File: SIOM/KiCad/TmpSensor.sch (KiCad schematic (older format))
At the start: 3 parts, among them U201 DS2482-800

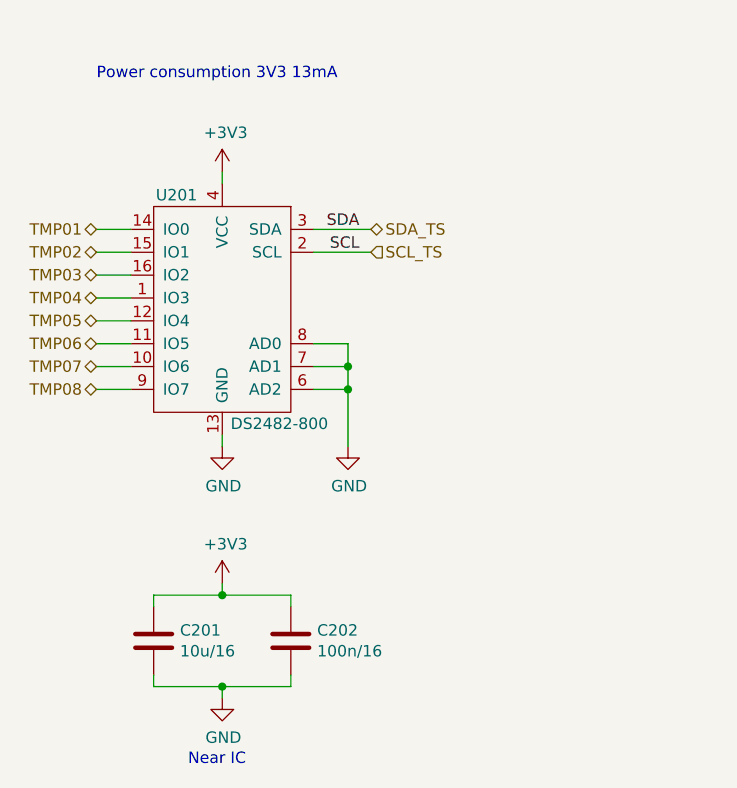
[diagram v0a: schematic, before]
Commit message: KiCad files SIOM_def
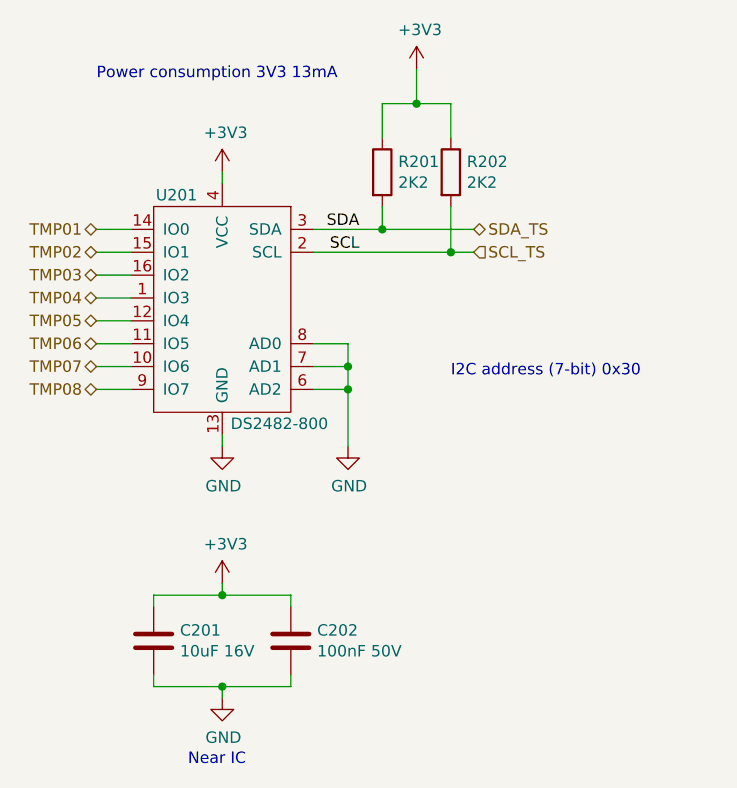
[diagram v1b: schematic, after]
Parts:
- added R201, R202: 2K2, Resistor_SMD:R_0603_1608Metric, symbol SIOMv01-rescue:R-Device
- C201: value 10u/16 -> 10uF 16V
- C202: value 100n/16 -> 100nF 50V
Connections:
- net +3V3: now also R201.1, R202.1
- net SCL_TS: now also R202.2
- net SDA_TS: now also R201.2
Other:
- note added: "I2C address (7-bit) 0x30"
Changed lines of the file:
@@
 EESchema Schematic File Version 4
-LIBS:SIOMv01-cache
 EELAYER 30 0
 EELAYER END
 $Descr A4 11693 8268
 encoding utf-8
-Sheet 2 9
+Sheet 2 10
 Title ""
 Date ""
@@
 $EndComp
 $Comp
-L SIOMv01-rescue:GND-power #PWR0203
+L SIOMv01-rescue:GND-power #PWR0205
 U 1 1 5FB29A98
 P 6600 4200
-F 0 "#PWR0203" H 6600 3950 50  0001 C CNN
+F 0 "#PWR0205" H 6600 3950 50  0001 C CNN
 F 1 "GND" H 6605 4027 50  0000 C CNN
 F 2 "" H 6600 4200 50  0001 C CNN
@@
 AR Path="/5F8C23BC/5FB2DA93" Ref="C201"  Part="1"
 F 0 "C201" H 5865 5096 50  0000 L CNN
-F 1 "10u/16" H 5865 5005 50  0000 L CNN
+F 1 "10uF 16V" H 5865 5005 50  0000 L CNN
 F 2 "Capacitor_SMD:C_0805_2012Metric" H 5788 4900 50  0001 C CNN
 F 3 "~" H 5750 5050 50  0001 C CNN
@@
 AR Path="/5FB2DA99" Ref="#PWR?"  Part="1"
 AR Path="/5F8BACBE/5FB2DA99" Ref="#PWR?"  Part="1"
-AR Path="/5F8C23BC/5FB2DA99" Ref="#PWR0205"  Part="1"
-F 0 "#PWR0205" H 6050 5050 50  0001 C CNN
+AR Path="/5F8C23BC/5FB2DA99" Ref="#PWR0204"  Part="1"
+F 0 "#PWR0204" H 6050 5050 50  0001 C CNN
 F 1 "GND" H 6055 5127 50  0000 C CNN
 F 2 "" H 6050 5300 50  0001 C CNN
@@
 P 6050 4800
 AR Path="/5F8BACBE/5FB2DAA1" Ref="#PWR?"  Part="1"
-AR Path="/5F8C23BC/5FB2DAA1" Ref="#PWR0204"  Part="1"
-F 0 "#PWR0204" H 6050 4650 50  0001 C CNN
+AR Path="/5F8C23BC/5FB2DAA1" Ref="#PWR0203"  Part="1"
+F 0 "#PWR0203" H 6050 4650 50  0001 C CNN
 F 1 "+3V3" H 6065 4973 50  0000 C CNN
 F 2 "" H 6050 4800 50  0001 C CNN
@@
 AR Path="/5F8C23BC/5FB6A68F" Ref="C202"  Part="1"
 F 0 "C202" H 6465 5096 50  0000 L CNN
-F 1 "100n/16" H 6465 5005 50  0000 L CNN
+F 1 "100nF 50V" H 6465 5005 50  0000 L CNN
 F 2 "Capacitor_SMD:C_0603_1608Metric" H 6388 4900 50  0001 C CNN
 F 3 "~" H 6350 5050 50  0001 C CNN
@@
 Text Notes 5900 5600 0    50   ~ 0
 Near IC
-Text HLabel 6700 3350 2    50   Input ~ 0
+Text HLabel 7150 3350 2    50   Input ~ 0
 SCL_TS
 Text Label 6650 3250 2    50   ~ 0
@@
 SCL
 Wire Wire Line
-	6450 3350 6700 3350
-Wire Wire Line
-	6450 3250 6700 3250
-Text HLabel 6700 3250 2    50   BiDi ~ 0
+	6450 3350 7050 3350
+Wire Wire Line
+	6450 3250 6750 3250
+Text HLabel 7150 3250 2    50   BiDi ~ 0
 SDA_TS
+$Comp
+L SIOMv01-rescue:R-Device R201
+U 1 1 6077B12F
+P 6750 3000
+F 0 "R201" H 6820 3046 50  0000 L CNN
+F 1 "2K2" H 6820 2955 50  0000 L CNN
+F 2 "Resistor_SMD:R_0603_1608Metric" V 6680 3000 50  0001 C CNN
+F 3 "~" H 6750 3000 50  0001 C CNN
+	1    6750 3000
+	1    0    0    -1
+$EndComp
+$Comp
+L SIOMv01-rescue:R-Device R202
+U 1 1 6077BA72
+P 7050 3000
+F 0 "R202" H 7120 3046 50  0000 L CNN
+F 1 "2K2" H 7120 2955 50  0000 L CNN
+F 2 "Resistor_SMD:R_0603_1608Metric" V 6980 3000 50  0001 C CNN
+F 3 "~" H 7050 3000 50  0001 C CNN
+	1    7050 3000
+	1    0    0    -1
+$EndComp
+Wire Wire Line
+	6750 3150 6750 3250
+Connection ~ 6750 3250
+Wire Wire Line
+	6750 3250 7150 3250
+Wire Wire Line
+	7050 3150 7050 3350
+Connection ~ 7050 3350
+Wire Wire Line
+	7050 3350 7150 3350
+Wire Wire Line
+	6750 2850 6750 2700
+Wire Wire Line
+	6750 2700 6900 2700
+Wire Wire Line
+	7050 2700 7050 2850
+Wire Wire Line
+	6900 2700 6900 2550
+Connection ~ 6900 2700
+Wire Wire Line
+	6900 2700 7050 2700
+$Comp
+L SIOMv01-rescue:+3V3-power #PWR0206
+U 1 1 6077D351
+P 6900 2550
+F 0 "#PWR0206" H 6900 2400 50  0001 C CNN
+F 1 "+3V3" H 6915 2723 50  0000 C CNN
+F 2 "" H 6900 2550 50  0001 C CNN
+F 3 "" H 6900 2550 50  0001 C CNN
+	1    6900 2550
+	1    0    0    -1
+$EndComp
+Text Notes 7050 3900 0    50   ~ 0
+I2C address (7-bit) 0x30
 $EndSCHEMATC
